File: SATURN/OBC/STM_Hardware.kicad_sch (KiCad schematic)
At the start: 10 parts, among them J1 SWD Pins, J2 USB_OTG, U1 USBLC6-4SC6, U2 RV-3028-C7 32.768KHZ 1PPM-TA-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

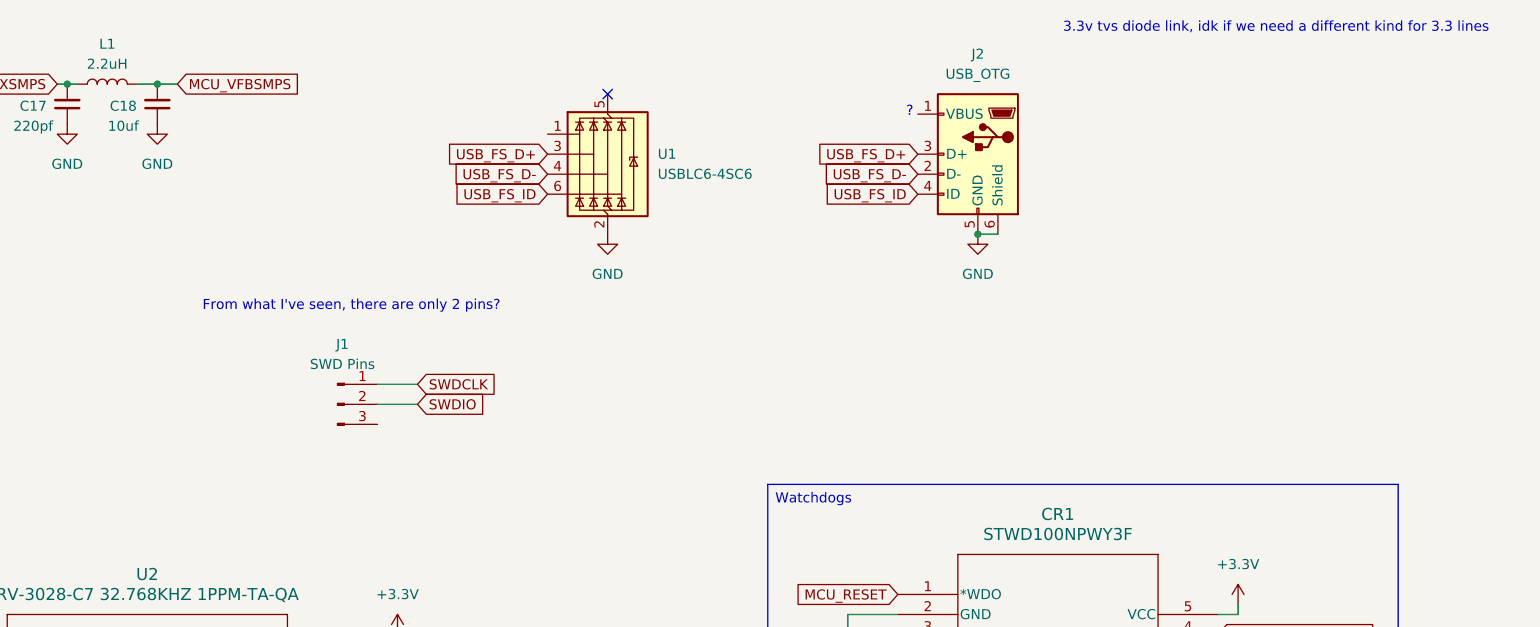
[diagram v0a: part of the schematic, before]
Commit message: Adding in SWD updates and box around
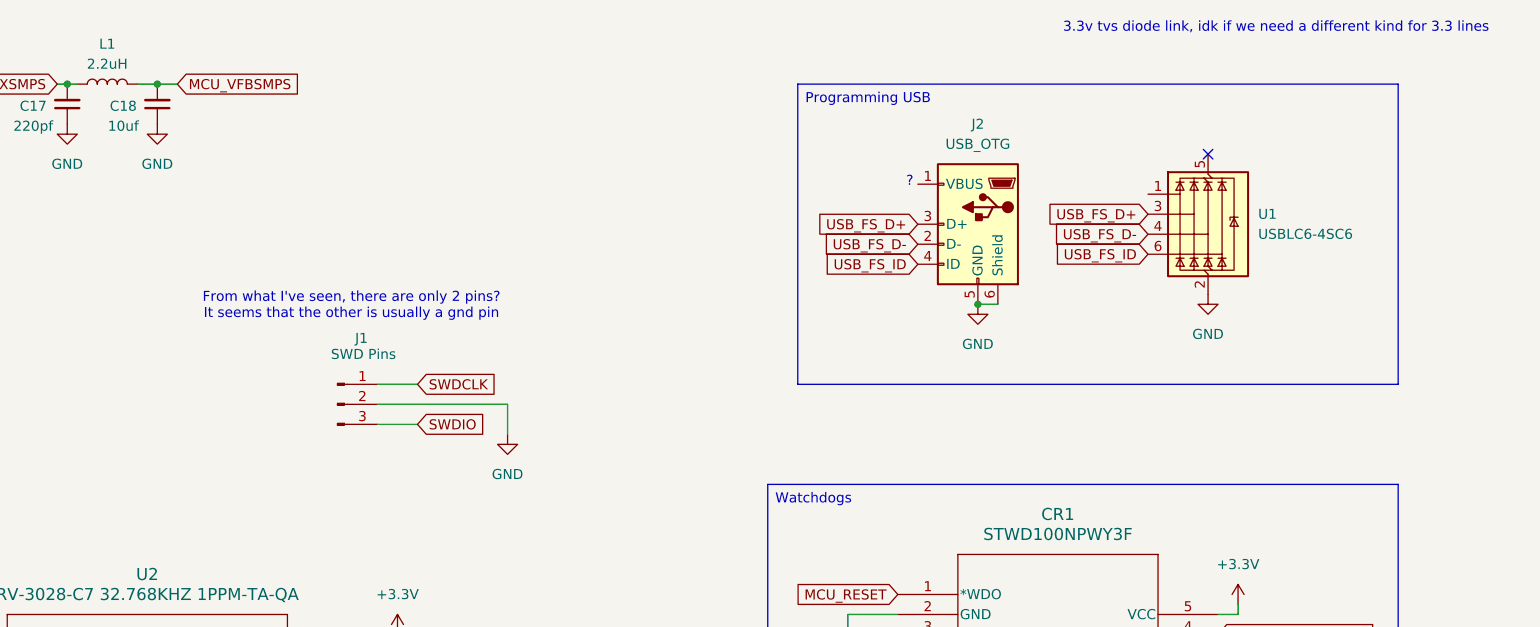
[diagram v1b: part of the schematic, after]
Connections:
- net GND: now also J1.2 (Pin_2)
- net SWDIO: now also J1.3 (Pin_3); no longer J1.2 (Pin_2)
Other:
- note added: "From what I've seen, there are only 2 pins? It seems that the other is usually a gnd pin"
- note removed: "From what I've seen, there are only 2 pins?"
- moved on the sheet: J2, U1
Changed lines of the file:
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@@
 		)
 	)
-	(text "From what I've seen, there are only 2 pins?\n"
+	(text "From what I've seen, there are only 2 pins?\nIt seems that the other is usually a gnd pin"
 		(exclude_from_sim no)
 		(at 137.668 49.784 0)
@@
 	(text "?"
 		(exclude_from_sim no)
-		(at 208.534 25.146 0)
+		(at 208.534 34.036 0)
 		(effects
 			(font
 				(size 1.27 1.27)
 			)
+		)
+	)
+	(text_box "Programming USB"
+		(exclude_from_sim no)
+		(at 194.31 21.59 0)
+		(size 76.2 38.1)
+		(margins 0.9525 0.9525 0.9525 0.9525)
+		(stroke
+			(width 0)
+			(type solid)
+		)
+		(fill
+			(type none)
+		)
+		(effects
+			(font
+				(size 1.27 1.27)
+			)
+			(justify left top)
 		)
 	)
@@
 	)
 	(junction
-		(at 217.17 40.64)
+		(at 217.17 49.53)
 		(diameter 0)
 		(color 0 0 0 0)
@@
 	)
 	(no_connect
-		(at 170.18 22.86)
+		(at 246.38 30.48)
 	)
 	(no_connect
@@
 	(wire
 		(pts
+			(xy 140.97 64.77) (xy 146.05 64.77)
+		)
+		(stroke
+			(width 0)
+			(type default)
+		)
+	)
+	(wire
+		(pts
 			(xy 207.01 88.9) (xy 200.66 88.9)
 		)
@@
 	(wire
 		(pts
-			(xy 140.97 62.23) (xy 146.05 62.23)
-		)
-		(stroke
-			(width 0)
-			(type default)
-		)
-	)
-	(wire
-		(pts
 			(xy 200.66 113.03) (xy 200.66 115.57)
 		)
@@
 	(wire
 		(pts
+			(xy 140.97 62.23) (xy 157.48 62.23)
+		)
+		(stroke
+			(width 0)
+			(type default)
+		)
+	)
+	(wire
+		(pts
 			(xy 115.57 21.59) (xy 113.03 21.59)
 		)
@@
 	(wire
 		(pts
-			(xy 217.17 40.64) (xy 219.71 40.64)
+			(xy 217.17 49.53) (xy 219.71 49.53)
 		)
 		(stroke
@@
 		(pts
 			(xy 143.51 91.44) (xy 143.51 96.52)
+		)
+		(stroke
+			(width 0)
+			(type default)
+		)
+	)
+	(wire
+		(pts
+			(xy 157.48 62.23) (xy 157.48 66.04)
 		)
 		(stroke
@@
 	(global_label "USB_FS_ID"
 		(shape input)
-		(at 162.56 35.56 180)
+		(at 238.76 43.18 180)
 		(fields_autoplaced yes)
 		(effects
@@
 		)
 		(property "Intersheetrefs" "${INTERSHEET_REFS}"
-			(at 149.6567 35.56 0)
+			(at 225.8567 43.18 0)
 			(hide yes)
 			(show_name no)
@@
 	(global_label "USB_FS_D+"
 		(shape input)
-		(at 162.56 30.48 180)
+		(at 238.76 38.1 180)
 		(fields_autoplaced yes)
 		(effects
@@
 		)
 		(property "Intersheetrefs" "${INTERSHEET_REFS}"
-			(at 148.6891 30.48 0)
+			(at 224.8891 38.1 0)
 			(hide yes)
 			(show_name no)
@@
 	(global_label "USB_FS_D-"
 		(shape input)
-		(at 209.55 33.02 180)
+		(at 209.55 41.91 180)
 		(fields_autoplaced yes)
 		(effects
@@
 		)
 		(property "Intersheetrefs" "${INTERSHEET_REFS}"
-			(at 195.6791 33.02 0)
+			(at 195.6791 41.91 0)
 			(hide yes)
 			(show_name no)
@@
 	(global_label "SWDIO"
 		(shape input)
-		(at 146.05 62.23 0)
+		(at 146.05 64.77 0)
 		(fields_autoplaced yes)
 		(effects
@@
 		)
 		(property "Intersheetrefs" "${INTERSHEET_REFS}"
-			(at 154.9014 62.23 0)
+			(at 154.9014 64.77 0)
 			(hide yes)
 			(show_name no)
@@
 	(global_label "USB_FS_D-"
 		(shape input)
-		(at 162.56 33.02 180)
+		(at 238.76 40.64 180)
 		(fields_autoplaced yes)
 		(effects
@@
 		)
 		(property "Intersheetrefs" "${INTERSHEET_REFS}"
-			(at 148.6891 33.02 0)
+			(at 224.8891 40.64 0)
 			(hide yes)
 			(show_name no)
@@
 	(global_label "USB_FS_D+"
 		(shape input)
-		(at 209.55 30.48 180)
+		(at 209.55 39.37 180)
 		(fields_autoplaced yes)
 		(effects
@@
 		)
 		(property "Intersheetrefs" "${INTERSHEET_REFS}"
-			(at 195.6791 30.48 0)
+			(at 195.6791 39.37 0)
 			(hide yes)
 			(show_name no)
@@
 	(global_label "USB_FS_ID"
 		(shape input)
-		(at 209.55 35.56 180)
+		(at 209.55 44.45 180)
 		(fields_autoplaced yes)
 		(effects
@@
 		)
 		(property "Intersheetrefs" "${INTERSHEET_REFS}"
-			(at 196.6467 35.56 0)
+			(at 196.6467 44.45 0)
 			(hide yes)
 			(show_name no)
@@
 	(symbol
 		(lib_id "power:GND")
-		(at 170.18 40.64 0)
+		(at 246.38 48.26 0)
 		(unit 1)
 		(body_style 1)
@@
 		(fields_autoplaced yes)
 		(property "Reference" "#PWR08"
-			(at 170.18 46.99 0)
+			(at 246.38 54.61 0)
 			(hide yes)
 			(show_name no)
@@
 		)
 		(property "Value" "GND"
-			(at 170.18 45.72 0)
+			(at 246.38 53.34 0)
 			(show_name no)
 			(do_not_autoplace no)
@@
 		)
 		(property "Footprint" ""
-			(at 170.18 40.64 0)
+			(at 246.38 48.26 0)
 			(hide yes)
 			(show_name no)
@@
 		)
 		(property "Datasheet" ""
-			(at 170.18 40.64 0)
+			(at 246.38 48.26 0)
 			(hide yes)
 			(show_name no)
@@
 		)
 		(property "Description" "Power symbol creates a global label with name \"GND\" , ground"
-			(at 170.18 40.64 0)
+			(at 246.38 48.26 0)
 			(hide yes)
 			(show_name no)
@@
 		(in_pos_files yes)
 		(dnp no)
-		(fields_autoplaced yes)
 		(property "Reference" "J1"
-			(at 136.525 54.61 0)
+			(at 138.938 53.848 0)
 			(show_name no)
 			(do_not_autoplace no)
@@
 		)
 		(property "Value" "SWD Pins"
-			(at 136.525 57.15 0)
+			(at 139.192 55.88 0)
 			(show_name no)
 			(do_not_autoplace no)
@@
 	(symbol
 		(lib_id "Power_Protection:USBLC6-4SC6")
-		(at 170.18 30.48 0)
+		(at 246.38 38.1 0)
 		(unit 1)
 		(body_style 1)
@@
 		(dnp no)
 		(property "Reference" "U1"
-			(at 176.53 30.4799 0)
+			(at 252.73 38.0999 0)
 			(show_name no)
 			(do_not_autoplace no)
@@
 		)
 		(property "Value" "USBLC6-4SC6"
-			(at 176.53 33.0199 0)
+			(at 252.73 40.6399 0)
 			(show_name no)
 			(do_not_autoplace no)
@@
 		)
 		(property "Footprint" "Package_TO_SOT_SMD:SOT-23-6"
-			(at 172.72 40.64 0)
+			(at 248.92 48.26 0)
 			(hide yes)
 			(show_name no)
@@
 		)
 		(property "Datasheet" "https://www.st.com/resource/en/datasheet/usblc6-4.pdf"
-			(at 172.72 43.18 0)
+			(at 248.92 50.8 0)
 			(hide yes)
 			(show_name no)
@@
 		)
 		(property "Description" "Very low capacitance ESD protection diode, 4 data-line, SOT-23-6"
-			(at 170.18 30.48 0)
+			(at 246.38 38.1 0)
 			(hide yes)
 			(show_name no)
@@
 	(symbol
 		(lib_id "Connector:USB_OTG")
-		(at 217.17 30.48 0)
+		(at 217.17 39.37 0)
 		(mirror y)
 		(unit 1)
@@
 		(dnp no)
 		(property "Reference" "J2"
-			(at 217.17 17.78 0)
+			(at 217.17 26.67 0)
 			(show_name no)
 			(do_not_autoplace no)
@@
 		)
 		(property "Value" "USB_OTG"
-			(at 217.17 20.32 0)
+			(at 217.17 29.21 0)
 			(show_name no)
 			(do_not_autoplace no)
@@
 		)
 		(property "Footprint" ""
-			(at 213.36 31.75 0)
+			(at 213.36 40.64 0)
 			(hide yes)
 			(show_name no)
@@
 		)
 		(property "Datasheet" ""
-			(at 213.36 31.75 0)
+			(at 213.36 40.64 0)
 			(hide yes)
 			(show_name no)
@@
 		)
 		(property "Description" "USB mini/micro connector"
-			(at 217.17 30.48 0)
+			(at 217.17 39.37 0)
 			(hide yes)
 			(show_name no)
@@
 				(path "/100d4475-6c5b-4ca4-82f4-ff20798e9edf/dc03155b-7cbf-4ee4-9f4c-dba3ed8dc3dd"
 					(reference "#PWR017")
+					(unit 1)
+				)
+			)
+		)
+	)
+	(symbol
+		(lib_id "power:GND")
+		(at 157.48 66.04 0)
+		(unit 1)
+		(body_style 1)
+		(exclude_from_sim no)
+		(in_bom yes)
+		(on_board yes)
+		(in_pos_files yes)
+		(dnp no)
+		(fields_autoplaced yes)
+		(property "Reference" "#PWR020"
+			(at 157.48 72.39 0)
+			(hide yes)
+			(show_name no)
+			(do_not_autoplace no)
+			(effects
+				(font
+					(size 1.27 1.27)
+				)
+			)
+		)
+		(property "Value" "GND"
+			(at 157.48 71.12 0)
+			(show_name no)
+			(do_not_autoplace no)
+			(effects
+				(font
+					(size 1.27 1.27)
+				)
+			)
+		)
+		(property "Footprint" ""
+			(at 157.48 66.04 0)
+			(hide yes)
+			(show_name no)
+			(do_not_autoplace no)
+			(effects
+				(font
+					(size 1.27 1.27)
+				)
+			)
+		)
+		(property "Datasheet" ""
+			(at 157.48 66.04 0)
+			(hide yes)
+			(show_name no)
+			(do_not_autoplace no)
+			(effects
+				(font
+					(size 1.27 1.27)
+				)
+			)
+		)
+		(property "Description" "Power symbol creates a global label with name \"GND\" , ground"
+			(at 157.48 66.04 0)
+			(hide yes)
+			(show_name no)
+			(do_not_autoplace no)
+			(effects
+				(font
+					(size 1.27 1.27)
+				)
+			)
+		)
+		(pin "1"
+		)
+		(instances
+			(project "OBC"
+				(path "/100d4475-6c5b-4ca4-82f4-ff20798e9edf/dc03155b-7cbf-4ee4-9f4c-dba3ed8dc3dd"
+					(reference "#PWR020")
 					(unit 1)
 				)
@@
 	(symbol
 		(lib_id "power:GND")
-		(at 217.17 40.64 0)
+		(at 217.17 49.53 0)
 		(unit 1)
 		(body_style 1)
@@
 		(fields_autoplaced yes)
 		(property "Reference" "#PWR09"
-			(at 217.17 46.99 0)
+			(at 217.17 55.88 0)
 			(hide yes)
 			(show_name no)
@@
 		)
 		(property "Value" "GND"
-			(at 217.17 45.72 0)
+			(at 217.17 54.61 0)
 			(show_name no)
 			(do_not_autoplace no)
@@
 		)
 		(property "Footprint" ""
-			(at 217.17 40.64 0)
+			(at 217.17 49.53 0)
 			(hide yes)
 			(show_name no)
@@
 		)
 		(property "Datasheet" ""
-			(at 217.17 40.64 0)
+			(at 217.17 49.53 0)
 			(hide yes)
 			(show_name no)
@@
 		)
 		(property "Description" "Power symbol creates a global label with name \"GND\" , ground"
-			(at 217.17 40.64 0)
-			(hide yes)
-			(show_name no)
+			(at 217.17 49.53 0)
+			(hide yes)
+			(show_name no)

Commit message: updating stuff
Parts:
- removed C17: 220pf, Capacitor_SMD:C_0603_1608Metric, symbol Device:C_Small
- removed C18: 10uf, Capacitor_SMD:C_0603_1608Metric, symbol Device:C_Small
- removed L1: 2.2uH, symbol Device:L

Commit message: Buncha changes, had to merge manually, hopefully nothing is broken.
Added the second MCU
Updated USB switcher
Added backup battery to RTC
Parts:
- removed CR1, CR2: STWD100NPWY3F, SOT23-5L_STM, symbol OBC-Components:STWD100NPWY3F
- removed J1: SWD Pins, symbol Connector:Conn_01x03_Pin
- removed J2: USB_OTG, symbol Connector:USB_OTG
- removed R1: 10 kOhm, symbol Device:R_Small_US
- removed U1: USBLC6-4SC6, Package_TO_SOT_SMD:SOT-23-6, symbol Power_Protection:USBLC6-4SC6
- removed U2: RV-3028-C7 32.768KHZ 1PPM-TA-QA, RV-3028-C7_MCX, symbol OBC-Components:RV-3028-C7_32.768KHZ_1PPM-TA-QA
- added B1: WA-BCPH, WA-BCPH:WA-BCPH_79578211, symbol OBC-Components-lin:WA-BCPH
- added C27: 220pf, Capacitor_SMD:C_0603_1608Metric, symbol Device:C_Small
- added C28: 10uf, Capacitor_SMD:C_0603_1608Metric, symbol Device:C_Small
- added CR3, CR4: STWD100NPWY3F, SOT23-5L_STM, symbol OBC-Components:STWD100NPWY3F
- added J3: SWD Pins, Connector_PinHeader_1.27mm:PinHeader_1x03_P1.27mm_Vertical, symbol Connector:Conn_01x03_Pin
- added J4: USB_OTG, symbol Connector:USB_OTG
- added JP1, JP2: Jumper_2_Open, symbol Jumper:Jumper_2_Open
- added L3: 2.2uH, symbol Device:L
- added R2, R3: 20kΩ, symbol Device:R_US
- added U3: RV-3028-C7 32.768KHZ 1PPM-TA-QA, RV-3028-C7_MCX, symbol OBC-Components:RV-3028-C7_32.768KHZ_1PPM-TA-QA
- added U4: TS3USB221ARSER, RSE10, symbol OBC-Components-lin:TS3USB221ARSER
- added U5: USBLC6-4SC6, Package_TO_SOT_SMD:SOT-23-6, symbol Power_Protection:USBLC6-4SC6
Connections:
- net +3.3V: now also CR3.5 (VCC), CR4.5 (VCC), JP1.1 (A), JP2.1 (A), U3.7 (VDD), U4.10 (VCC)
- net GND: now also B1.-, C27.1, C28.1, CR3.2 (GND), CR3.3 (*EN), CR4.2 (GND), CR4.3 (*EN), J3.2 (Pin_2), J4.5 (GND), J4.6 (Shield), R2.2, R3.1, U3.5 (VSS), U3.8 (EVI), U4.5 (GND), U5.2 (GND)
- net MCU_1_WATCHDOG: now also CR3.4 (WDI)
- net MCU_2_WATCHDOG: now also CR4.4 (WDI)
- net MCU_CLK: now also U3.1 (CLKOUT)
- net MCU_RESET: now also CR3.1 (*WDO), CR4.1 (*WDO)
- net SCL: now also U3.3 (SCL)
- net SDA: now also U3.4 (SDA)
- net SWDCLK: now also J3.1 (Pin_1)
- net SWDIO: now also J3.3 (Pin_3)
- net USB_FS_D+: now also J4.3 (D+), U4.8 (D+), U5.3 (I/O2)
- net USB_FS_D-: now also J4.2 (D-), U4.7 (D-), U5.4 (I/O3)
- new net: JP1.2 (B), R3.2, U4.9 (S)
- new net: JP2.2 (B), R2.1, U4.6 (*OE)
- new net: B1.+, U3.6 (VBACKUP)
- new net MCU1_USB_FS_D+: U4.1 (1D+)
- new net MCU1_USB_FS_D-: U4.2 (1D-)
- new net MCU2_USB_FS_D+: U4.3 (2D+)
- new net MCU2_USB_FS_D-: U4.4 (2D-)
- new net MCU_VFBSMPS: C28.2, L3.2
- new net MCU_VLXSMPS: C27.2, L3.1
- no-connect marks 2 -> 4
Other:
- removed sheet MCU Power
- removed sheet STM32H7 MCU
- added sheet MCU Power1 (MCU_Power.kicad_sch)
- added sheet STM32H7 MCU1 (STM32H7 MCU.kicad_sch)
- note added: "Open by default to allow programming (pull high to turn off)"
- note added: "The backup battery is a generic rechargeable C2350 button battery"
- note removed: "The RTC has a backup voltage allowed but we don't need it, so I tied it to gnd with 10kOhm as per datasheet"
